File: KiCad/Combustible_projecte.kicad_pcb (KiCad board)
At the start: 2 copper layers, 56 parts, among them J1 DE9_Pins, J2 DE9_Pins, J20 Conn_01x02, J3 Conn_01x05, J4 Conn_01x02, J5 Conn_01x02, J6 Conn_01x02, Q1 2N7002, Q2 2N7002, SW1 SW_Push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

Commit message: PnR Final versió 1
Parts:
- added REF**: MountingHole_2.1mm, MountingHole:MountingHole_2.1mm, F.Cu at (58.5, 26.0)
- added REF**: MountingHole_2.1mm, MountingHole:MountingHole_2.1mm, F.Cu at (177.0, 26.0)
- added REF**: MountingHole_2.1mm, MountingHole:MountingHole_2.1mm, F.Cu at (177.5, 95.5)
- added REF**: MountingHole_2.1mm, MountingHole:MountingHole_2.1mm, F.Cu at (58.0, 95.5)
- moved U2 168.4 mm to (81.5, 75.1), turned to 180 degrees
- moved D1 121.1 mm to (110.5, 82.9), turned to 90 degrees
- moved C10 120.6 mm to (102.5, 72.0), turned to -90 degrees
- moved R1 120.5 mm to (72.0, 76.0), turned to 90 degrees
- moved C1 116.3 mm to (80.5, 68.0), turned to 90 degrees
- moved J1 115.4 mm to (70.9, 84.0)
- moved SW1 111.7 mm to (138.0, 71.0), turned to 90 degrees
- moved C2 109.5 mm to (89.0, 75.0), turned to 180 degrees
- moved J5 104.8 mm to (158.0, 89.0)
- moved J3 102.8 mm to (97.5, 80.9)
- moved Y1 99.9 mm to (128.5, 84.6), turned to -90 degrees
- moved R2 94.2 mm to (102.0, 82.5)
- moved U3 93.8 mm to (152.6, 51.0)
- moved R5 91.1 mm to (97.5, 72.0), turned to 90 degrees
- moved R6 87.3 mm to (102.0, 77.5)
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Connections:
- C2 pad 2: Sortida_RL -> 3v3
- J3 pad 2: sortida_RL -> 3v3
- R1 pad 2: CAN_ L -> CAN_L
- U2 pad 5: Sortida_RL -> 3v3
- U2 pad 6: CAN_ L -> CAN_L
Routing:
- net GND: track 0.00 -> 124.8 mm, vias 0 -> 86
- net 3v3: track 0.00 -> 103.1 mm, vias 0 -> 13
- net CAN_TX: track 0.00 -> 68.3 mm
- net CAN_RX: track 0.00 -> 65.7 mm
- net USART_RX: track 0.00 -> 55.5 mm
- net PGD: track 0.00 -> 55.0 mm
- net PGC: track 0.00 -> 50.2 mm
- net USART_TX: track 0.00 -> 48.2 mm
- net RBO: track 0.00 -> 41.8 mm
- net Net-(U4-/MCLR): track 0.00 -> 30.8 mm
- net CAN_H: track 0.00 -> 18.4 mm
- net CAN_L: track 0.00 -> 18.2 mm
- net LED_p_n: track 0.00 -> 17.5 mm
- net /MCLR: track 0.00 -> 15.5 mm
- net R1_IN: track 0.00 -> 14.1 mm
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- added copper zone on F.Cu, net 3v3
- added copper zone on B.Cu, net GND
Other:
- board outline added: 125.5 x 75.5 mm

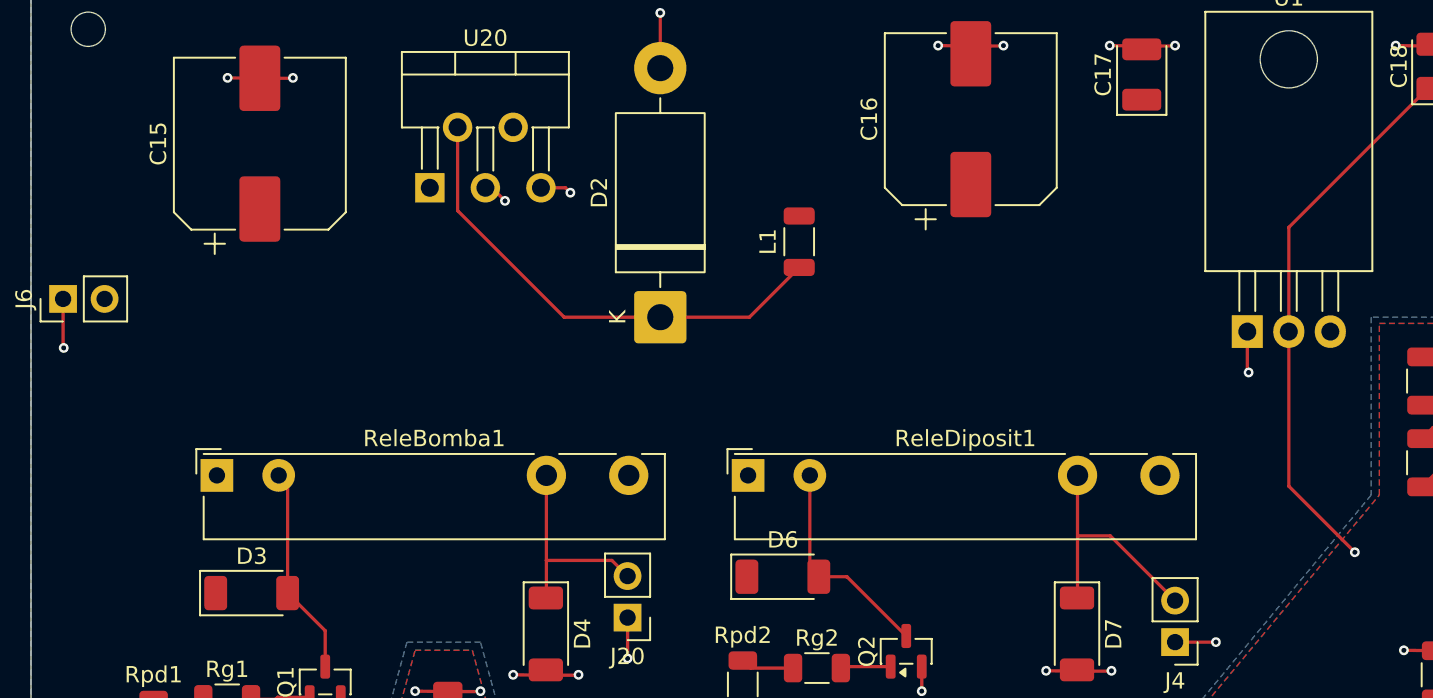
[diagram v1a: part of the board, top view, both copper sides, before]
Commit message: PnR Final versió 2, VBAT i 5V afegit
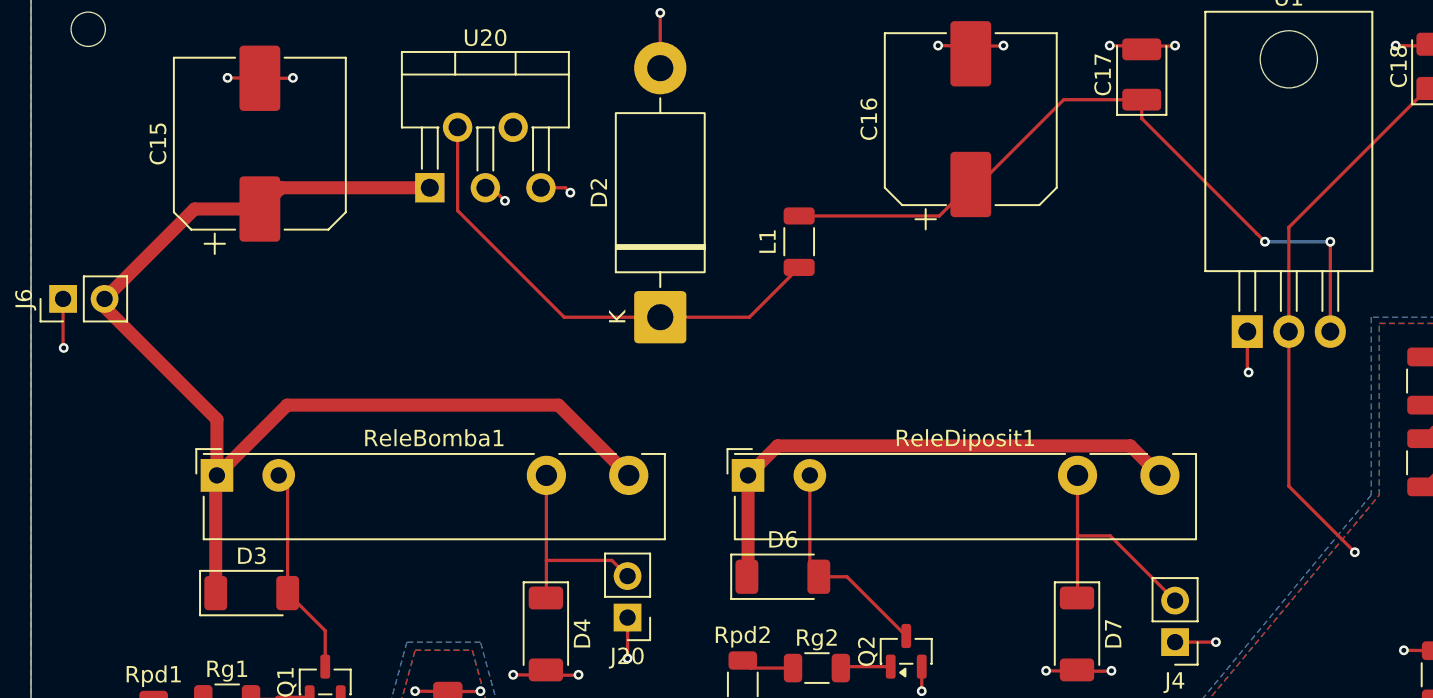
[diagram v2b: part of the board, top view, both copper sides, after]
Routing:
- net VBAT: track 0.00 -> 105.3 mm
- net 5v: track 0.00 -> 45.2 mm, vias 0 -> 2
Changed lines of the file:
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@@
+	)
+	(segment
+		(start 98.8725 59.4275)
+		(end 98.8 59.5)
+		(width 0.8)
+		(layer "F.Cu")
+		(net 13)
+	)
+	(segment
+		(start 69 37)
+		(end 70.3 35.7)
+		(width 0.8)
+		(layer "F.Cu")
+		(net 13)
+	)
+	(segment
+		(start 66.3725 49.8725)
+		(end 66.3725 53.2975)
+		(width 0.8)
+		(layer "F.Cu")
+		(net 13)
+	)
+	(segment
+		(start 98.8725 53.2975)
+		(end 100.6735 51.4965)
+		(width 0.8)
+		(layer "F.Cu")
+		(net 13)
+	)
+	(segment
+		(start 70.3 35.7)
+		(end 79.4 35.7)
+		(width 0.8)
+		(layer "F.Cu")
+		(net 13)
+	)
+	(segment
+		(start 100.6735 51.4965)
+		(end 122.2715 51.4965)
+		(width 0.8)
+		(layer "F.Cu")
+		(net 13)
+	)
+	(segment
+		(start 122.2715 51.4965)
+		(end 124.0725 53.2975)
+		(width 0.8)
+		(layer "F.Cu")
+		(net 13)
+	)
+	(segment
+		(start 65 37)
+		(end 69 37)
+		(width 0.8)
+		(layer "F.Cu")
+		(net 13)
+	)
+	(segment
+		(start 87.275 49)
+		(end 91.5725 53.2975)
+		(width 0.8)
+		(layer "F.Cu")
+		(net 13)
+	)
+	(segment
+		(start 66.3 60.5)
+		(end 66.3 53.37)
+		(width 0.8)
+		(layer "F.Cu")
+		(net 13)
+	)
+	(segment
+		(start 98.8725 53.2975)
+		(end 98.8725 59.4275)
+		(width 0.8)
+		(layer "F.Cu")
+		(net 13)
+	)
+	(segment
+		(start 59.5 42.5)
+		(end 65 37)
+		(width 0.8)
+		(layer "F.Cu")
+		(net 13)
+	)
+	(segment
+		(start 59.5 43)
+		(end 66.3725 49.8725)
+		(width 0.8)
+		(layer "F.Cu")
+		(net 13)
+	)
+	(segment
+		(start 66.3 53.37)
+		(end 66.3725 53.2975)
+		(width 0.8)
+		(layer "F.Cu")
+		(net 13)
+	)
+	(segment
+		(start 59.5 42.5)
+		(end 59.5 43)
+		(width 0.8)
+		(layer "F.Cu")
+		(net 13)
+	)
+	(segment
+		(start 66.3725 53.2975)
+		(end 70.67 49)
+		(width 0.8)
+		(layer "F.Cu")
+		(net 13)
+	)
+	(segment
+		(start 70.67 49)
+		(end 87.275 49)
+		(width 0.8)
+		(layer "F.Cu")
+		(net 13)
+	)
+	(segment
+		(start 122.96 31.46)
+		(end 130 38.5)
+		(width 0.2)
+		(layer "F.Cu")
+		(net 14)
+	)
+	(segment
+		(start 110.575 37.425)
+		(end 112.5 35.5)
+		(width 0.2)
+		(layer "F.Cu")
+		(net 14)
+	)
+	(segment
+		(start 134.5 39)
+		(end 134.5 44.5)
+		(width 0.2)
+		(layer "F.Cu")
+		(net 14)
+	)
+	(segment
+		(start 113 35.5)
+		(end 118.19 30.31)
+		(width 0.2)
+		(layer "F.Cu")
+		(net 14)
+	)
+	(segment
+		(start 102 37.425)
+		(end 110.575 37.425)
+		(width 0.2)
+		(layer "F.Cu")
+		(net 14)
+	)
+	(segment
+		(start 122.96 30.31)
+		(end 122.96 31.46)
+		(width 0.2)
+		(layer "F.Cu")
+		(net 14)
+	)
+	(segment
+		(start 130 38.5)
+		(end 130.5 39)
+		(width 0.2)
+		(layer "F.Cu")
+		(net 14)
+	)
+	(segment
+		(start 112.5 35.5)
+		(end 113 35.5)
+		(width 0.2)
+		(layer "F.Cu")
+		(net 14)
+	)
+	(segment
+		(start 118.19 30.31)
+		(end 122.96 30.31)
+		(width 0.2)
+		(layer "F.Cu")
+		(net 14)
+	)
+	(via
+		(at 130.5 39)
+		(size 0.6)
+		(drill 0.3)
+		(layers "F.Cu" "B.Cu")
+		(net 14)
+	)
+	(via
+		(at 134.5 39)
+		(size 0.6)
+		(drill 0.3)
+		(layers "F.Cu" "B.Cu")
+		(net 14)
+	)
+	(segment
+		(start 130.5 39)
+		(end 134.5 39)
+		(width 0.2)
+		(layer "B.Cu")
+		(net 14)
 	)
 	(segment

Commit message: pista de 5 volts incluida
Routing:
- net 5v: track 45.2 -> 65.0 mm
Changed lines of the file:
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@@
+	)
+	(segment
+		(start 96.575 32)
+		(end 102 37.425)
+		(width 0.2)
+		(layer "F.Cu")
+		(net 14)
 	)
 	(segment
@@
 		(width 0.2)
 		(layer "F.Cu")
+		(net 14)
+	)
+	(segment
+		(start 84.5 32)
+		(end 96.575 32)
+		(width 0.2)
+		(layer "F.Cu")

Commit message: pnr editat
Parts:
- J20, J4, J5, J6: footprint Connector_PinHeader_2.54mm:PinHeader_1x02_P2.54mm_Vertical -> TerminalBlock_TE-Connectivity:TerminalBlock_TE_282834-2_1x02_P2.54mm_Horizontal
- J3: footprint Connector_PinHeader_2.54mm:PinHeader_1x05_P2.54mm_Vertical -> TerminalBlock_TE-Connectivity:TerminalBlock_TE_282834-5_1x05_P2.54mm_Horizontal
- moved D4 104.8 mm to (-11.0, 24.5)
- moved D6 104.8 mm to (3.50, 21.0)
- moved D7 104.8 mm to (21.5, 24.5)
- moved Q2 104.8 mm to (11.1, 25.6)
- moved Rg2 104.8 mm to (5.59, 26.6)
- moved Rpd2 104.8 mm to (1.05, 27.6)
- moved C18 50.9 mm to (97.5, 55.5)
- moved C17 50.3 mm to (80.0, 55.0), turned to -90 degrees
- moved C16 49.3 mm to (72.5, 60.3), turned to 180 degrees
- moved J20 45.9 mm to (121.1, 26.9), turned to 90 degrees
- moved J4 37.8 mm to (136.4, 27.5), turned to -90 degrees
- moved U1 37.1 mm to (92.5, 48.3), turned to 180 degrees
- moved ReleBomba1 35.8 mm to (89.5, 26.0)
- moved D3 34.0 mm to (37.8, 75.0)
- moved Q1 34.0 mm to (42.3, 80.4)
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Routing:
- net VBAT: track 105.3 -> 0.00 mm
- net 5v: track 65.0 -> 0.00 mm, vias 2 -> 0
- net GND: track 124.8 -> 91.1 mm, vias 86 -> 76
- net Net-(D2-K): track 30.0 -> 0.00 mm
- net 3v3: track 103.1 -> 75.2 mm
- net Diposit: track 15.1 -> 0.00 mm
- net Bomba_combustible: track 12.9 -> 0.00 mm
- net Net-(D6-A): track 13.3 -> 1.07 mm
- net Net-(D3-A): track 12.9 -> 5.45 mm
- added copper zone on F.Cu, net 5v
- added copper zone on F.Cu, net GND
- added copper zone on F.Cu, net VBAT
- removed copper zone on B.Cu, net GND

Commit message: millora routing
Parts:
- moved D4 118.5 mm to (107.5, 25.0), turned to 0 degrees
- moved D7 94.0 mm to (115.2, 32.4), turned to 90 degrees
- moved Rpd2 76.1 mm to (77.0, 32.0), turned to 90 degrees
- moved Rg2 75.7 mm to (81.0, 33.0)
- moved D6 75.2 mm to (78.6, 25.6)
- moved C12 70.4 mm to (97.4, 46.9), turned to 90 degrees
- moved Q2 69.8 mm to (80.7, 29.2)
- moved D3 54.2 mm to (72.0, 33.0), turned to 180 degrees
- moved Rg1 53.4 mm to (59.6, 33.4)
- moved Q1 53.3 mm to (65.6, 32.5)
- moved Rpd1 51.7 mm to (58.0, 38.5)
- moved R1 46.0 mm to (118.0, 77.0)
- moved U2 42.4 mm to (123.9, 76.8)
- moved C13 39.4 mm to (111.4, 46.7)
- moved C11 37.4 mm to (108.6, 46.7)
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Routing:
- net 3v3: track 75.2 -> 4.72 mm, vias 13 -> 0
- net GND: track 91.1 -> 39.8 mm, vias 76 -> 77
- net CAN_RX: track 65.7 -> 17.3 mm, vias 0 -> 2
- net CAN_TX: track 68.3 -> 21.6 mm, vias 0 -> 2
- net CAN_L: track 18.2 -> 55.2 mm
- net CAN_H: track 18.4 -> 53.3 mm
- net Net-(U4-/MCLR): track 30.8 -> 3.89 mm
- net RBO: track 41.8 -> 15.0 mm
- net Bomba_combustible: track 0.00 -> 20.6 mm
- net USART_RX: track 55.5 -> 36.7 mm, vias 0 -> 2
- net PGC: track 50.2 -> 31.5 mm
- net PGD: track 55.0 -> 37.0 mm
- net Diposit: track 0.00 -> 17.1 mm
- net Net-(D2-K): track 0.00 -> 17.0 mm
- net Net-(D6-A): track 1.07 -> 13.4 mm
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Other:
- board size 125.5 x 75.5 mm -> 103.1 x 69.4 mm

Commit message: millora pcb
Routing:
- net USART_TX: track 39.0 -> 32.3 mm
- net GND: track 39.8 -> 36.7 mm, vias 77 -> 76
- net USART_RX: track 36.7 -> 34.1 mm, vias 2 -> 4
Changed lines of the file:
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@@
-	)
-	(segment
-		(start 73.44 69.32)
-		(end 73.44 68.36)
-		(width 0.2)
-		(layer "F.Cu")
-		(net 2)
 	)
 	(segment
@@
 	)
 	(segment
-		(start 71.9 70.86)
-		(end 73.44 69.32)
-		(width 0.2)
-		(layer "F.Cu")
-		(net 2)
-	)
-	(segment
 		(start 127.4 33.525)
 		(end 126.075 33.525)
@@
 	)
 	(via
-		(at 73.44 68.36)
-		(size 0.6)
-		(drill 0.3)
-		(layers "F.Cu" "B.Cu")
-		(net 2)
-	)
-	(via
 		(at 99.8 46.5875)
 		(size 0.6)
@@
 	)
 	(segment
+		(start 132.8 61.604968)
+		(end 132.8 47.2)
+		(width 0.2)
+		(layer "F.Cu")
+		(net 54)
+	)
+	(segment
+		(start 129.215968 65.189)
+		(end 132.8 61.604968)
+		(width 0.2)
+		(layer "F.Cu")
+		(net 54)
+	)
+	(segment
 		(start 129.645332 45.705)
 		(end 130.620331 45.705)
@@
 	)
 	(segment
-		(start 132.8 54.738)
-		(end 136.569 50.969)
+		(start 126.824 65.449032)
+		(end 127.084032 65.189)
 		(width 0.2)
 		(layer "F.Cu")
@@
 	)
 	(segment
-		(start 129.215968 65.189)
-		(end 132.8 61.604968)
+		(start 132.8 47.2)
+		(end 131.305 45.705)
 		(width 0.2)
 		(layer "F.Cu")
@@
 	)
 	(segment
-		(start 136.569 50.969)
-		(end 131.305 45.705)
+		(start 126.824 70.568999)
+		(end 126.824 65.449032)
+		(width 0.2)
+		(layer "F.Cu")
+		(net 54)
+	)
+	(segment
+		(start 127.125001 70.87)
+		(end 126.824 70.568999)
+		(width 0.2)
+		(layer "F.Cu")
+		(net 54)
+	)
+	(segment
+		(start 131.305 45.705)
+		(end 130.620331 45.705)
 		(width 0.2)
 		(layer "F.Cu")
@@
 	)
 	(segment
-		(start 127.109 48.241332)
-		(end 129.645332 45.705)
-		(width 0.2)
-		(layer "F.Cu")
-		(net 54)
-	)
-	(segment
-		(start 131.305 45.705)
-		(end 130.620331 45.705)
-		(width 0.2)
-		(layer "F.Cu")
-		(net 54)
-	)
-	(segment
-		(start 126.824 70.568999)
-		(end 126.824 65.449032)
-		(width 0.2)
-		(layer "F.Cu")
-		(net 54)
-	)
-	(segment
-		(start 127.125001 70.87)
-		(end 126.824 70.568999)
-		(width 0.2)
-		(layer "F.Cu")
-		(net 54)
-	)
-	(segment
 		(start 127.084032 65.189)
 		(end 129.215968 65.189)
@@
 	)
 	(segment
-		(start 126.824 65.449032)
-		(end 127.084032 65.189)
-		(width 0.2)
-		(layer "F.Cu")
-		(net 54)
-	)
-	(segment
-		(start 132.8 61.604968)
-		(end 132.8 54.738)
-		(width 0.2)
-		(layer "F.Cu")
-		(net 54)
-	)
-	(segment
-		(start 135.8115 64.2)
-		(end 135.8115 64.138443)
+		(start 131.578219 61.978219)
+		(end 131.6 61.956438)
 		(width 0.2)
 		(layer "F.Cu")
@@
 	)
 	(segment
-		(start 131.235 44.435)
-		(end 130.620331 44.435)
+		(start 133.8 49)
+		(end 133.8 45.6)
 		(width 0.2)
 		(layer "F.Cu")
@@
 	)
 	(segment
-		(start 135.7865 61.62734)
-		(end 135.7865 54.2135)
-		(width 0.2)
-		(layer "F.Cu")
-		(net 55)
-	)
-	(segment
-		(start 135.7865 54.2135)
-		(end 138.4 51.6)
-		(width 0.2)
-		(layer "F.Cu")
-		(net 55)
-	)
-	(segment
-		(start 131.8 65.61384)
-		(end 135.7865 61.62734)
+		(start 133.8 45.6)
+		(end 132.635 44.435)
 		(width 0.2)
 		(layer "F.Cu")
@@
 	)
 	(segment
-		(start 138.4 51.6)
-		(end 131.235 44.435)
-		(width 0.2)
-		(layer "F.Cu")
-		(net 55)
-	)
-	(segment
-		(start 131.8 66.6)
-		(end 131.8 65.61384)
-		(width 0.2)
-		(layer "F.Cu")
-		(net 55)
-	)
-	(segment
 		(start 128.15 72.14)
 		(end 130.06 72.14)
@@
 		(net 55)
 	)
+	(segment
+		(start 131.6 61.956438)
+		(end 131.6 50.6)
+		(width 0.2)
+		(layer "F.Cu")
+		(net 55)
+	)
+	(segment
+		(start 132.635 44.435)
+		(end 130.620331 44.435)
+		(width 0.2)
+		(layer "F.Cu")
+		(net 55)
+	)
+	(via
+		(at 131.578219 61.978219)
+		(size 0.6)
+		(drill 0.3)
+		(layers "F.Cu" "B.Cu")
+		(net 55)
+	)
 	(via
 		(at 131.4 70.8)
@@
 	)
 	(via
-		(at 131.8 66.6)
+		(at 133.8 49)
 		(size 0.6)
 		(drill 0.3)
@@
 		(net 55)
 	)
+	(via
+		(at 131.6 50.6)
+		(size 0.6)
+		(drill 0.3)
+		(layers "F.Cu" "B.Cu")
+		(net 55)
+	)
+	(segment
+		(start 131.6 50.6)
+		(end 132.2 50.6)
+		(width 0.2)
+		(layer "B.Cu")
+		(net 55)
+	)
+	(segment
+		(start 132.2 50.6)
+		(end 133.8 49)
+		(width 0.2)
+		(layer "B.Cu")
+		(net 55)
+	)
 	(segment
 		(start 131.4 67)
-		(end 131.8 66.6)
+		(end 131.4 62)
+		(width 0.2)
+		(layer "B.Cu")
+		(net 55)
+	)
+	(segment
+		(start 131.4 62)
+		(end 131.556438 62)
+		(width 0.2)
+		(layer "B.Cu")
+		(net 55)
+	)
+	(segment
+		(start 131.556438 62)
+		(end 131.578219 61.978219)
 		(width 0.2)
 		(layer "B.Cu")
@@
 		(polygon
 			(pts
-				(xy 54.5 23.4) (xy 54.6 50.9) (xy 112.9 49.8) (xy 112.6 22.7)
+				(xy 55.7 24.6) (xy 56 50.9) (xy 112.2 50.6) (xy 112.4 23.9)
 			)
 		)
@@
 		(polygon
 			(pts
-				(xy 54.575 23.05) (xy 54.975 92.75) (xy 158.175 92.25) (xy 157.875 22.55)
+				(xy 54.575 21.25) (xy 54.975 92.75) (xy 158.175 92.25) (xy 157.875 20.75)
 			)
 		)

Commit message: millora pcb
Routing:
- net Net-(D1-A): track 8.81 -> 7.18 mm
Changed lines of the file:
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@@
 	)
 	(segment
-		(start 104.097114 54.172057)
-		(end 101 54.172057)
+		(start 101 56.312557)
+		(end 102.751057 54.5615)
 		(width 0.2)
 		(layer "F.Cu")
@@
 	)
 	(segment
-		(start 101 54.172057)
-		(end 101 54.125)
+		(start 104.486556 54.5615)
+		(end 105.986057 56.061)
 		(width 0.2)
 		(layer "F.Cu")
@@
 	)
 	(segment
-		(start 105.986057 56.061)
-		(end 104.097114 54.172057)
+		(start 102.751057 54.5615)
+		(end 104.486556 54.5615)
 		(width 0.2)
 		(layer "F.Cu")
@@
 	(segment
 		(start 101 57.1625)
-		(end 101 54.172057)
+		(end 101 56.312557)
 		(width 0.2)
 		(layer "F.Cu")

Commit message: millora illa de coure a gnd
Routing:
- net GND: vias 76 -> 88
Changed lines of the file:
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@@
+	)
+	(via
+		(at 110.2 59.4)
+		(size 0.6)
+		(drill 0.3)
+		(layers "F.Cu" "B.Cu")
+		(free yes)
+		(net 2)
 	)
 	(via
@@
 	)
 	(via
+		(at 116.4 72.4)
+		(size 0.6)
+		(drill 0.3)
+		(layers "F.Cu" "B.Cu")
+		(free yes)
+		(net 2)
+	)
+	(via
 		(at 138.5 69.1)
 		(size 0.6)
@@
 	)
 	(via
+		(at 110.6 71.8)
+		(size 0.6)
+		(drill 0.3)
+		(layers "F.Cu" "B.Cu")
+		(free yes)
+		(net 2)
+	)
+	(via
 		(at 120.5 67.1)
 		(size 0.6)
@@
 	)
 	(via
+		(at 109.8 61)
+		(size 0.6)
+		(drill 0.3)
+		(layers "F.Cu" "B.Cu")
+		(free yes)
+		(net 2)
+	)
+	(via
 		(at 106.2 46.3875)
 		(size 0.6)
@@
 	)
 	(via
+		(at 110.2 59.4)
+		(size 0.6)
+		(drill 0.3)
+		(layers "F.Cu" "B.Cu")
+		(free yes)
+		(net 2)
+	)
+	(via
 		(at 80.55 57.7875)
 		(size 0.6)
@@
 	)
 	(via
+		(at 110.2 59.4)
+		(size 0.6)
+		(drill 0.3)
+		(layers "F.Cu" "B.Cu")
+		(free yes)
+		(net 2)
+	)
+	(via
 		(at 120.5 65.6)
 		(size 0.6)
@@
 	)
 	(via
+		(at 110.6 71.8)
+		(size 0.6)
+		(drill 0.3)
+		(layers "F.Cu" "B.Cu")
+		(free yes)
+		(net 2)
+	)
+	(via
 		(at 111.5 73.6)
 		(size 0.6)
@@
 	)
 	(via
+		(at 116.4 72.4)
+		(size 0.6)
+		(drill 0.3)
+		(layers "F.Cu" "B.Cu")
+		(free yes)
+		(net 2)
+	)
+	(via
 		(at 106 61.6)
 		(size 0.6)
@@
 	)
 	(via
+		(at 109.8 61)
+		(size 0.6)
+		(drill 0.3)
+		(layers "F.Cu" "B.Cu")
+		(free yes)
+		(net 2)
+	)
+	(via
 		(at 117 70.6)
 		(size 0.6)
@@
 	)
 	(via
+		(at 109.8 61)
+		(size 0.6)
+		(drill 0.3)
+		(layers "F.Cu" "B.Cu")
+		(free yes)
+		(net 2)
+	)
+	(via
 		(at 56.025 39.975)
 		(size 0.6)
@@
 	)
 	(via
+		(at 116.4 72.4)
+		(size 0.6)
+		(drill 0.3)
+		(layers "F.Cu" "B.Cu")
+		(free yes)
+		(net 2)
+	)
+	(via
 		(at 121.33 79.67)
 		(size 0.6)
@@
 		(net 2)
 	)
+	(via
+		(at 110.6 71.8)
+		(size 0.6)
+		(drill 0.3)
+		(layers "F.Cu" "B.Cu")
+		(free yes)
+		(net 2)
+	)
